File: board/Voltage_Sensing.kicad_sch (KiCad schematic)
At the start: 43 parts, among them U4 Opamp_Dual, U5 Opamp_Dual, U6 Opamp_Dual, U7 Opamp_Dual, U8 Opamp_Dual, U9 Opamp_Dual

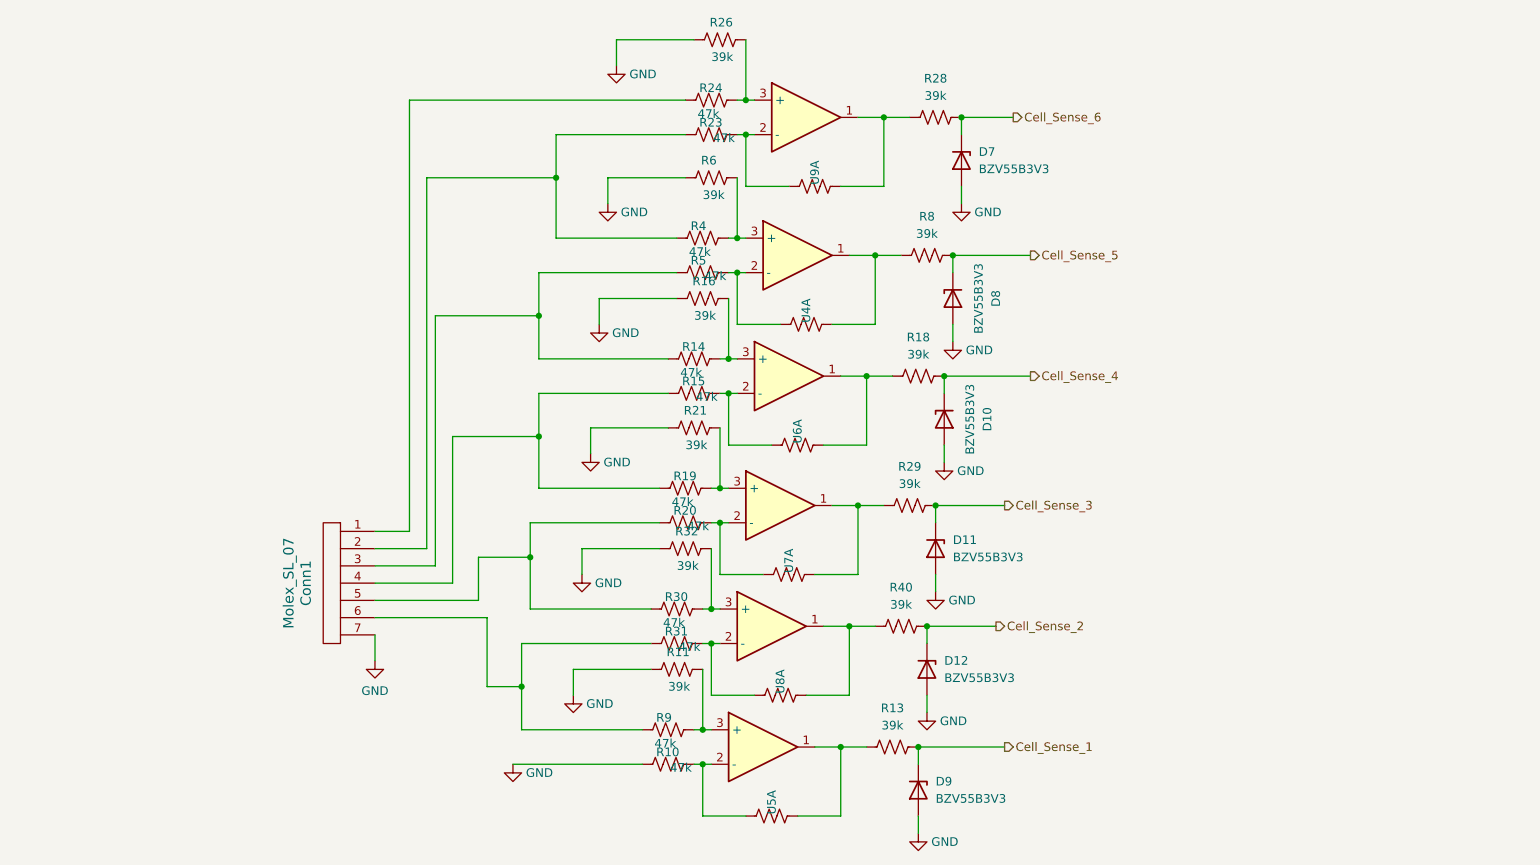
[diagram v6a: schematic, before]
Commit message: added fixes for schematic
redid op amp symbols
put Xs on teensy
Put andersons on current protection page
changed resistor value for buzzer
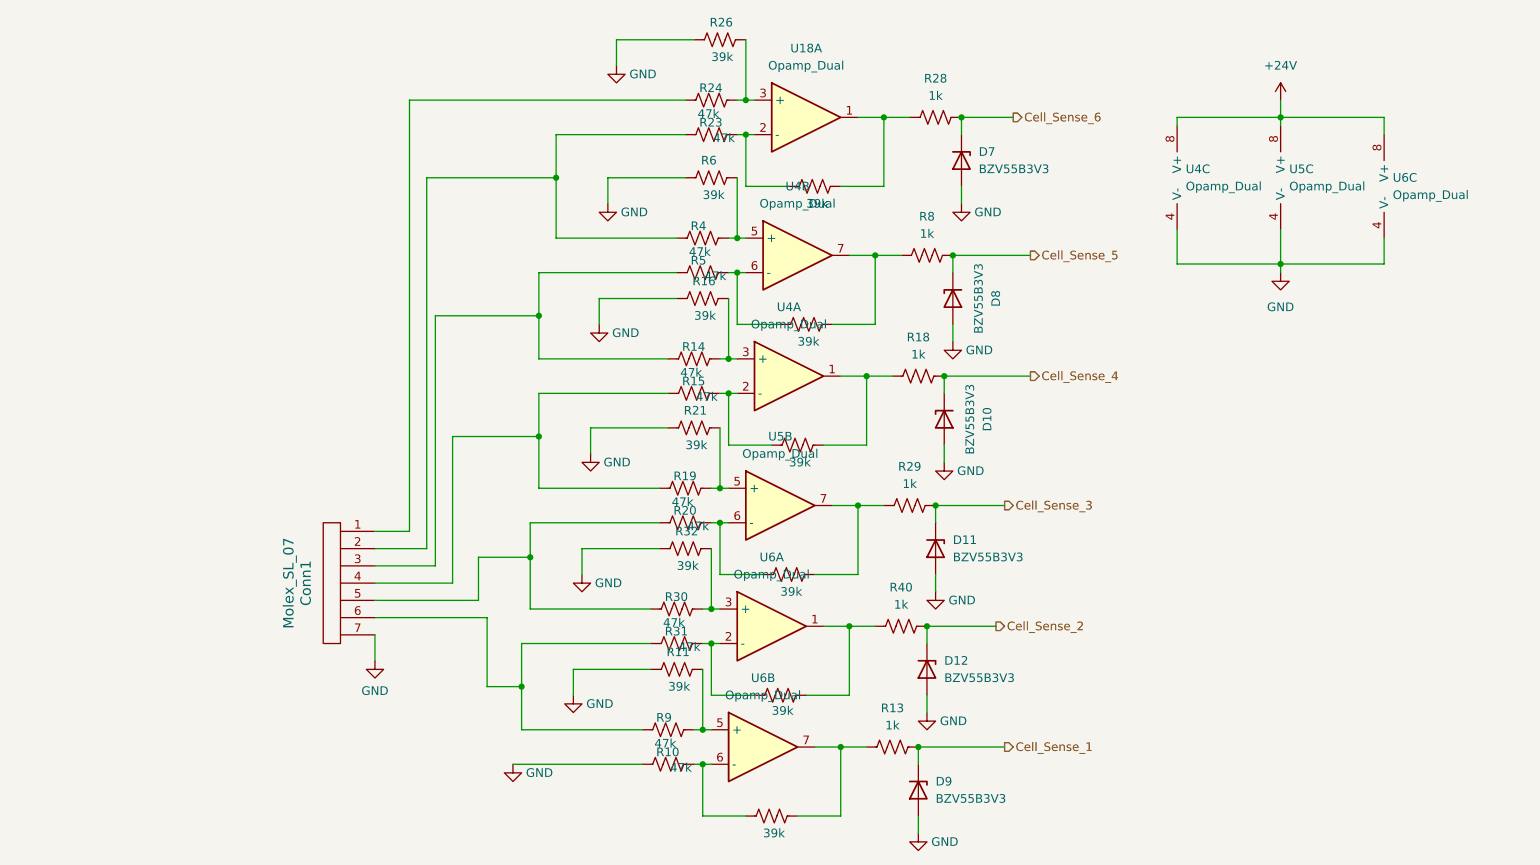
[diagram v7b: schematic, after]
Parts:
- removed U5, U7, U8, U9: Opamp_Dual, symbol Device:Opamp_Dual
- added U18, U5: Opamp_Dual, symbol Device:Opamp_Dual
- added unit 3 of U4
- added unit 2 of U4
- added unit 2 of U6
- added unit 3 of U6
- R13, R18, R28, R29, R40, R8: value 39k -> 1k
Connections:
- net GND: now also U4.4 (V-), U5.4 (V-), U6.4 (V-)
- net at R4.1, R6.1: now also U4.5 (+); no longer U4.3 (+)
- net at R30.1, R32.1: now also U6.3 (+)
- net at R25.1, R28.1: now also U18.1
- net at R23.1, R25.2: now also U18.2 (-)
- net at R24.1, R26.1: now also U18.3 (+)
- net at R33.1, R40.1: now also U6.1
- net at R12.1, R13.1: now also U6.7
- net at R10.1, R12.2: now also U6.6 (-)
- net at R31.1, R33.2: now also U6.2 (-)
- net at R7.1, R8.1: now also U4.7; no longer U4.1
- net at R5.1, R7.2: now also U4.6 (-); no longer U4.2 (-)
- net at R22.1, R29.1: now also U5.7
- net at R20.1, R22.2: now also U5.6 (-)
- net at R19.1, R21.1: now also U5.5 (+)
- net at R17.1, R18.1: now also U4.1; no longer U6.1
- net at R15.1, R17.2: now also U4.2 (-); no longer U6.2 (-)
- net at R14.1, R16.1: now also U4.3 (+); no longer U6.3 (+)
- net at R11.1, R9.1: now also U6.5 (+)
- new net +24V: U4.8 (V+), U5.8 (V+), U6.8 (V+)
